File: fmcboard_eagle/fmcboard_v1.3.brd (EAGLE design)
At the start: 147 x 74 mm, 128 parts, among them IC1 OPA699ID, IC10 LTC6229IMS8E#TRPBF, IC11 7805TV, IC12 7905, IC3 LTC6229IMS8E#TRPBF, IC4 LTC6229IMS8E#TRPBF, IC5 LM358, IC6 OPA699ID, IC7 OPA699ID, IC8 LTC6229IMS8E#TRPBF, IC9 LTC6229IMS8E#TRPBF, J1 8pin, J12 4p-2.54, J2 ASP-134604-01, J3 4p-2.54, J4 4p-2.54, J5 8pin, J6 4p-2.54, J7 4p-2.54, J8 4p-2.54, U1 TXS0108EPWR

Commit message: v1.3
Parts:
- R42: value 50 -> 50?
- moved IC12 1.00 mm to (92.0, 80.0)
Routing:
- net VS+: track 39.2 -> 352.8 mm, vias 0 -> 13
- net GND: track 0.00 -> 274.5 mm, vias 0 -> 25
- net 1V8: track 0.00 -> 168.0 mm, vias 0 -> 2
- net VH: track 2.84 -> 169.5 mm, vias 0 -> 6
- net VL: track 2.84 -> 151.4 mm, vias 0 -> 9
- net G36: track 0.00 -> 147.8 mm, vias 0 -> 3
- net G37: track 0.00 -> 126.3 mm, vias 0 -> 3
- net SDAIN: track 0.00 -> 124.9 mm, vias 0 -> 1
- net VS-: track 193.8 -> 318.3 mm, vias 0 -> 1
- net SCLIN: track 0.00 -> 106.1 mm, vias 0 -> 2
- net OPOUT1_H10: track 13.5 -> 112.0 mm, vias 0 -> 3
- net OFFSETOUT1: track 0.00 -> 92.5 mm, vias 0 -> 1
- net C10: track 0.00 -> 88.5 mm, vias 0 -> 1
- net OFFSETIN2: track 0.00 -> 88.2 mm, vias 0 -> 4
- net OPOUT2_H11: track 16.8 -> 102.0 mm, vias 0 -> 2
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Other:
- board text added: "C10GX FMC breakout, v1.3 by Andre Dubovskiy and Dr. Andy Haas NYU, 2023"
- board text removed: "C10GX FMC breakout, v1.21 by Andre Dubovskiy and Dr. Andy Haas NYU, 2023"

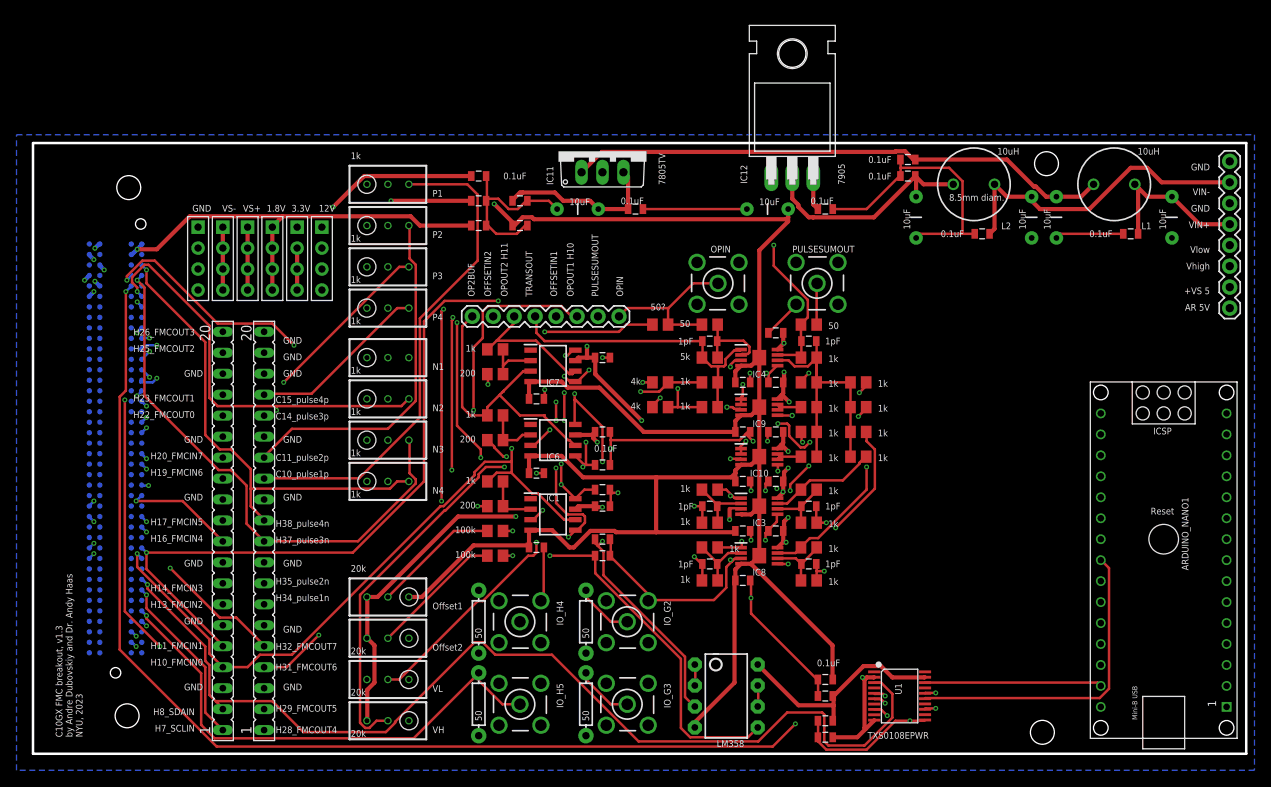
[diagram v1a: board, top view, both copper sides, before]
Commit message: Fix feedback compensation caps on neg pulse amps, new footprint for L7905
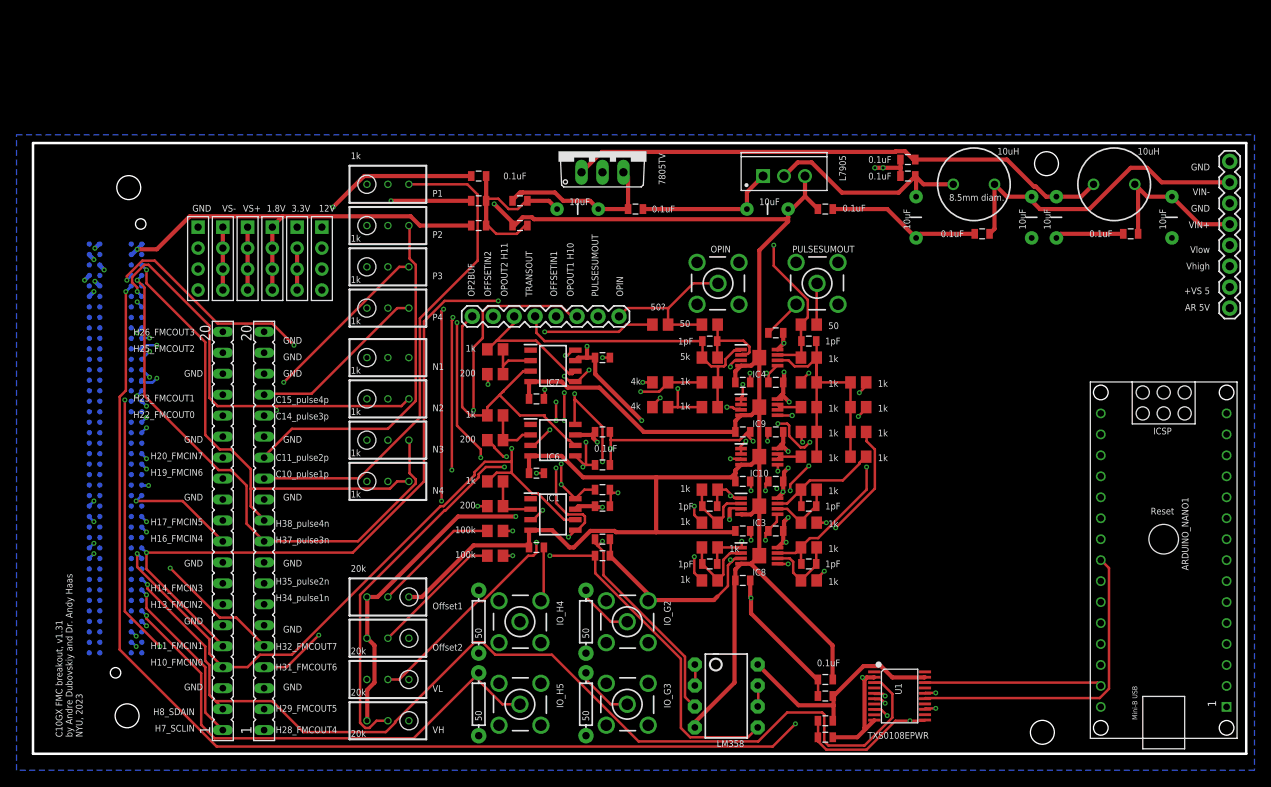
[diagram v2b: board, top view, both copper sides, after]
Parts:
- removed IC12: 7905, linear:TO220H
- added U2: STMICROELECTRONICS_L7905ACVSTMICROELECTRONICS_L7905ACV_0_0, STMicroelectronics - L7905ACV:STMICROELECTRONICS_L7905ACV_0
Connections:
- net GND: now also U2.1; no longer IC12.1
- net N$12: now also C35.1; no longer C35.2
- net N$13: now also C34.1; no longer C34.2
- net N$14: now also C37.2; no longer C37.1
- net N$4: now also C36.2; no longer C36.1
- net PULSEINN1: no longer C34.1
- net PULSEINN2: no longer C36.2
- net PULSEINN3: no longer C35.1
- net PULSEINN4: no longer C37.2
- net PULSEOUTN1: now also C34.2
- net PULSEOUTN2: now also C36.1
- net PULSEOUTN3: now also C35.2
- net PULSEOUTN4: now also C37.1
- net VIN-CLEAN: now also U2.2; no longer IC12.2
- net VS-: now also U2.3; no longer IC12.3
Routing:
- net GND: track 274.5 -> 285.0 mm, vias 25 -> 27
- net PULSEOUTN3: track 29.8 -> 31.8 mm
- net PULSEOUTN1: track 25.4 -> 27.4 mm
- net PULSEOUTN2: track 13.2 -> 15.2 mm
- net PULSEOUTN4: track 35.6 -> 37.7 mm
- net PULSEINN2: track 62.9 -> 60.9 mm
- net VS-: track 318.3 -> 316.4 mm
- net N$12: track 8.29 -> 10.1 mm
- net VIN-CLEAN: track 28.2 -> 26.5 mm
- net N$14: track 7.95 -> 9.50 mm
- net PULSEINN4: track 60.5 -> 59.1 mm
- net N$13: track 7.95 -> 9.30 mm
- net PULSEINN1: track 47.6 -> 47.0 mm
- net N$4: track 7.81 -> 8.35 mm
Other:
- board text added: "C10GX FMC breakout, v1.31 by Andre Dubovskiy and Dr. Andy Haas NYU, 2023"
- board text added: "L7905"
- board text removed: "C10GX FMC breakout, v1.3 by Andre Dubovskiy and Dr. Andy Haas NYU, 2023"
